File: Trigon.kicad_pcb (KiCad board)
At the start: 2 copper layers, 160 x 120 mm, 110 parts, among them J1 TYPE-C-31-M12_13, J2 TYPE-C-31-M12_13, SW1 SW_Push, SW2 Rotary_Encoder_Switch, U1 ATmega32U4-AU, U2 USBLC6-2SC6, U3 CY7C65632-28LTXCT, U4 USBLC6-2SC6, Y1 16MHz, Y2 12MHz

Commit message: next round of feedback from josh
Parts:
- removed D27, D28: 6V Breakdown, acheron_Components:D_SOD-123_Bidirectional
- moved R4 5.17 mm to (93.6, 20.6), turned to 0 degrees
- moved C2 2.06 mm to (146.3, 40.6)
- moved F1 1.83 mm to (96.6, 24.1)
- moved C21 1.83 mm to (97.4, 22.2)
- moved FB4 1.83 mm to (97.4, 26.0)
- moved C6 1.59 mm to (140.8, 44.2)
- moved C1 1.52 mm to (151.2, 43.2)
- moved R2 0.51 mm to (135.8, 56.4)
- moved R5 0.38 mm to (103.3, 23.4)
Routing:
- net +5V: track 237.0 -> 245.7 mm, vias 10 -> 9
- net GND: track 39.9 -> 48.3 mm, vias 28 -> 36
- net Net-(F1-Pad1): track 9.25 -> 2.84 mm
- net Net-(F2-Pad1): track 8.08 -> 2.50 mm
- net VBUS: track 19.0 -> 14.3 mm
- net Net-(J1-PadA5): track 3.65 -> 8.18 mm, vias 0 -> 2
- net ROW0: track 167.7 -> 170.9 mm, vias 6 -> 4
- net D3_D+: track 42.6 -> 44.5 mm
- net D3_D-: track 46.0 -> 47.9 mm
- net Net-(C2-Pad1): track 10.3 -> 8.68 mm
- net Net-(C1-Pad1): track 8.72 -> 7.19 mm
- net Net-(R10-Pad1): track 15.4 -> 16.2 mm
- net VREG_3V3: track 37.3 -> 38.2 mm
- net COL6: track 21.5 -> 22.3 mm
- net Net-(D13-Pad2): track 14.5 -> 15.3 mm
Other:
- board text added: "rev 0.1"
- board text removed: "rev 0"

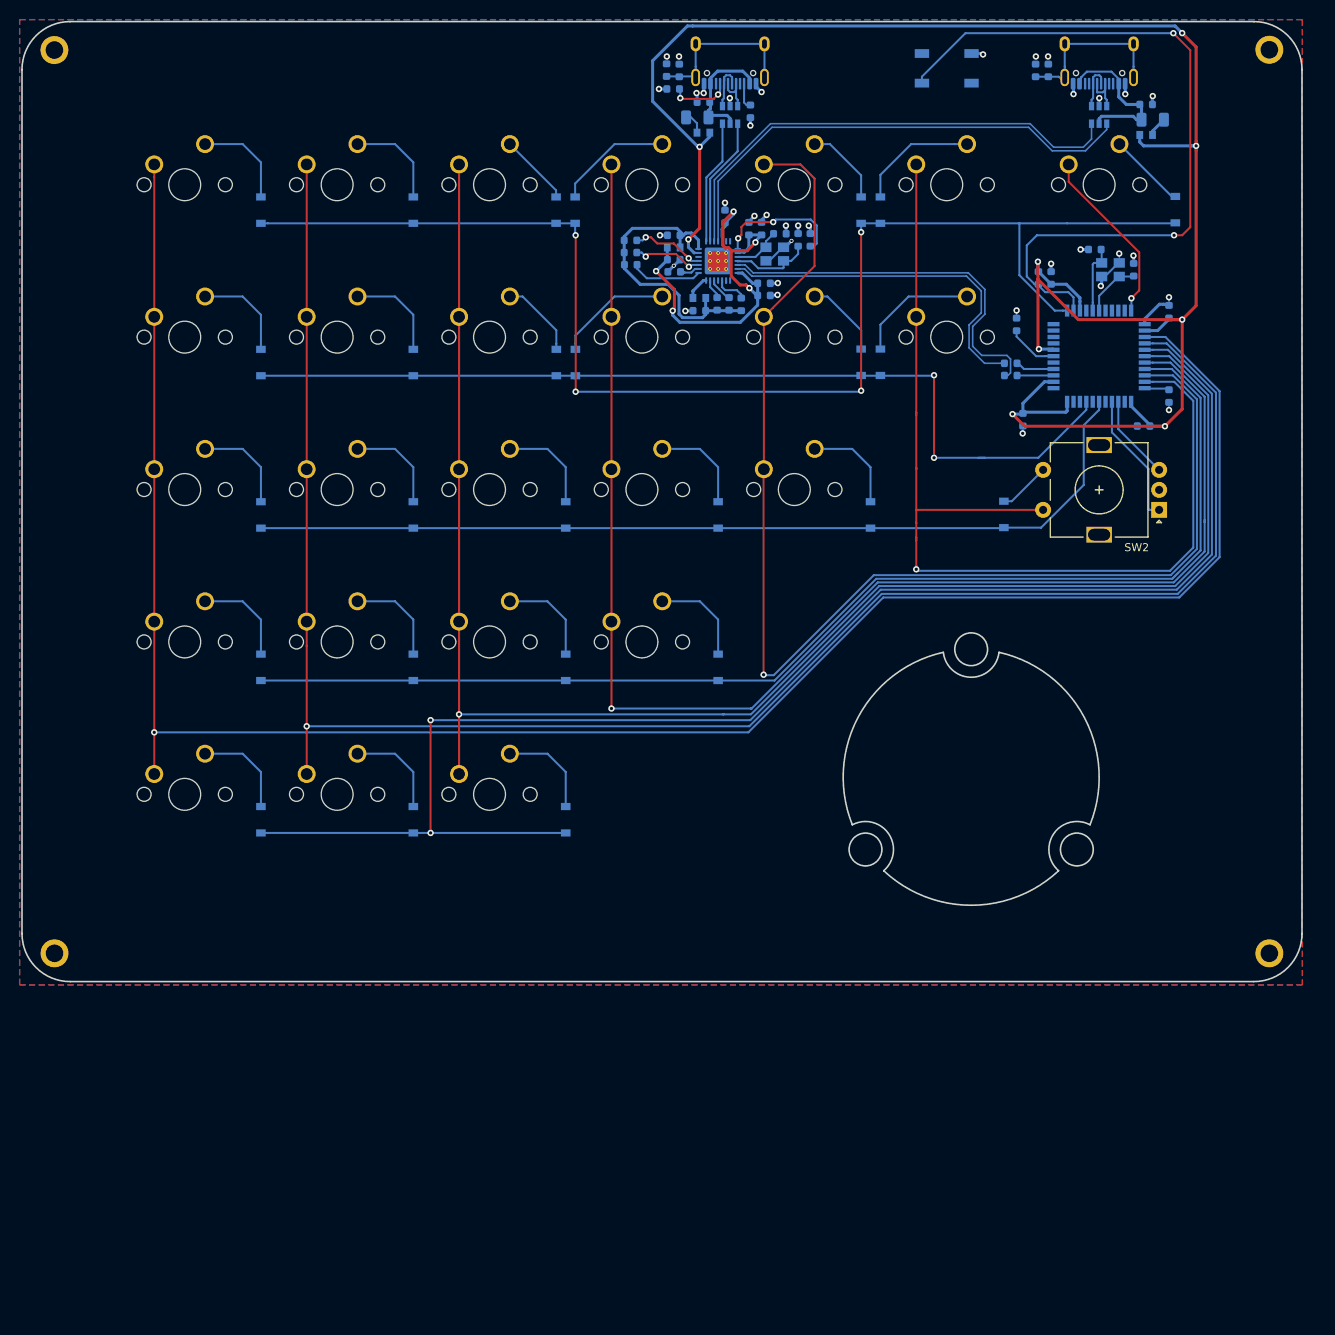
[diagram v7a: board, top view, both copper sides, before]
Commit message: - Introduced JST connector - Made all D+/D- 14mm thick (max thickness that was easy to deal with) - Added logo / decoration / version #
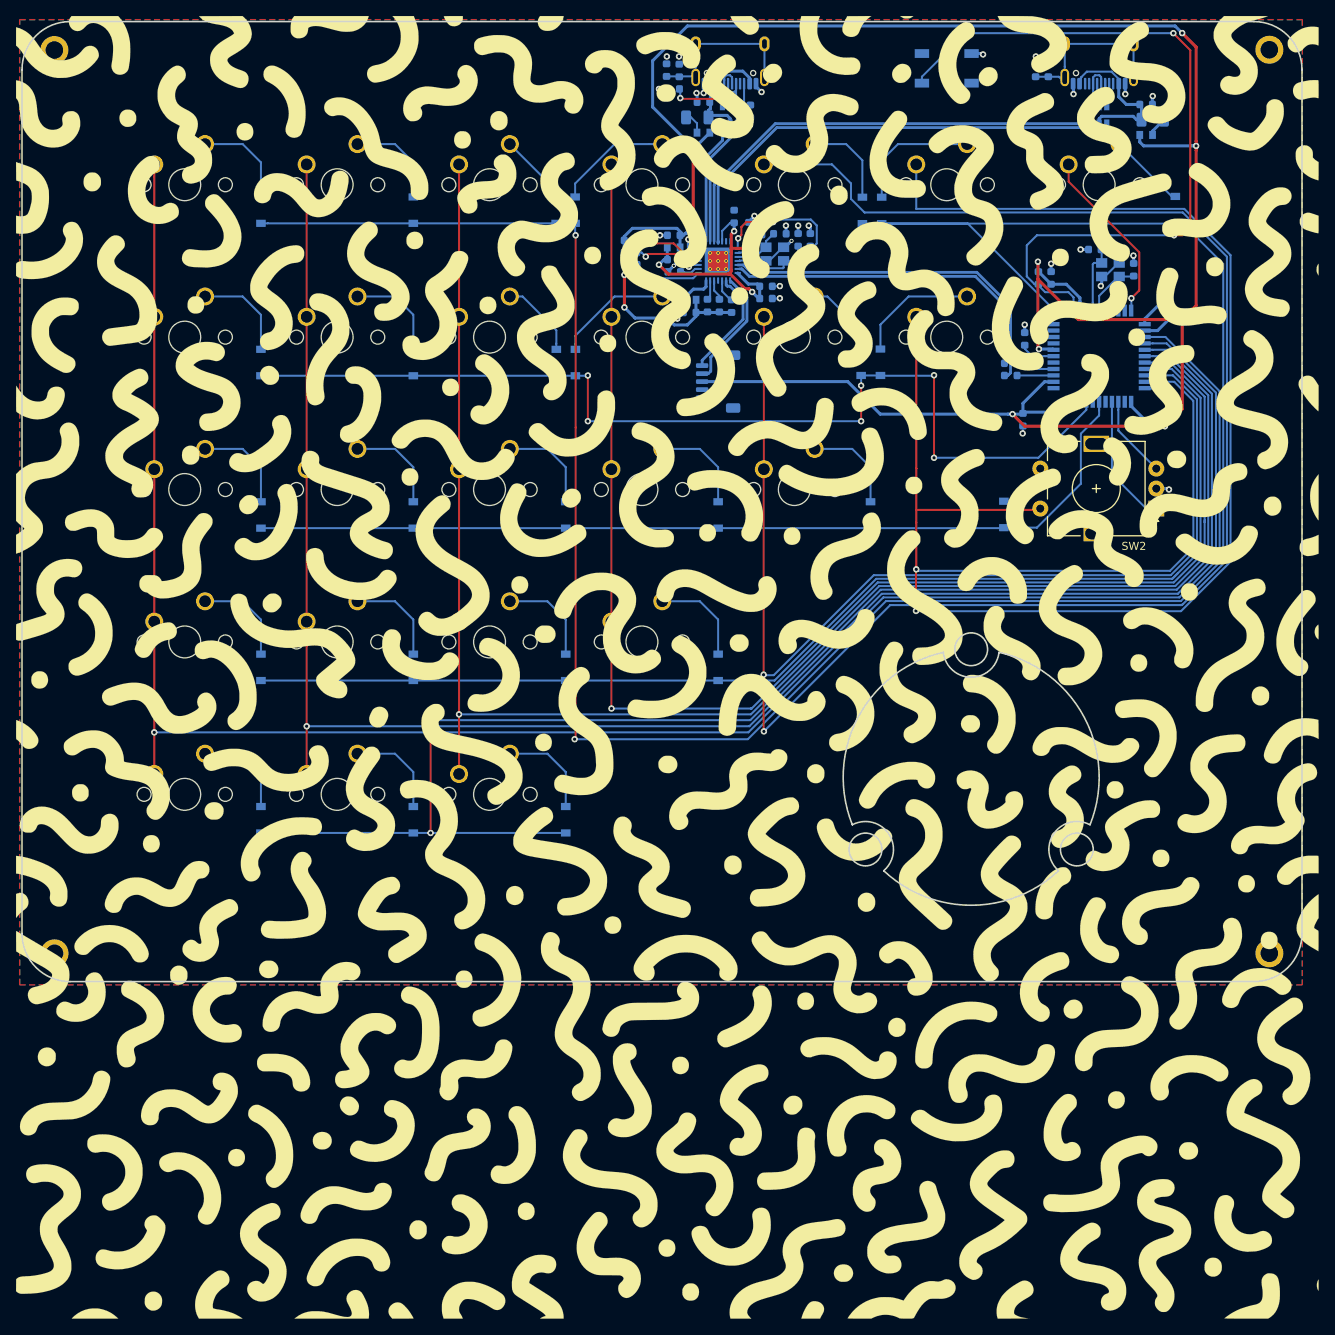
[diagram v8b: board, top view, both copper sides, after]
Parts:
- added H1: Logo, Trigon:wiggle, F.Cu at (92.9, 92.9)
- added J3: Conn_01x05, Connector_JST:JST_SH_SM05B-SRSS-TB_1x05-1MP_P1.00mm_Horizontal, B.Cu at (99.2, 57.1)
- SW2: footprint Keebio-Parts:RotaryEncoder_Alps_EC11E-Switch_Vertical_H20mm -> Rotary_Encoder:RotaryEncoder_Alps_EC11E-Switch_Vertical_H20mm
- moved SW2 7.52 mm to (154.0, 73.0)
- moved C3 2.08 mm to (137.5, 51.8)
- moved R13 1.23 mm to (97.9, 47.7)
- moved R14 1.23 mm to (99.4, 47.7)
- moved R9 1.23 mm to (100.9, 47.7)
- moved C8 1.23 mm to (95.7, 48.5)
- moved FB1 1.23 mm to (95.7, 46.9)
- moved C13 1.14 mm to (101.2, 36.5)
- moved C16 0.46 mm to (105.2, 46.8)
- moved C17 0.46 mm to (105.2, 45.2)
- moved D5 0.16 mm to (117.3, 35.8)
- moved D6 0.16 mm to (119.7, 35.8)
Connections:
- U3 pad 15: Net-(U3-Pad15) -> D2_D-
- U3 pad 16: Net-(U3-Pad16) -> D2_D+
- U3 pad 6: D2_D- -> Net-(U3-Pad6)
- U3 pad 7: D2_D+ -> Net-(U3-Pad7)
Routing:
- net COL4: track 159.8 -> 308.7 mm, vias 1 -> 2
- net ROW0: track 170.9 -> 306.1 mm, vias 4 -> 2
- net COL5: track 128.8 -> 242.9 mm, vias 1 -> 2
- net +5V: track 245.7 -> 286.3 mm
- net D2_D-: track 0.00 -> 15.3 mm
- net D2_D+: track 0.00 -> 13.8 mm
- net +3.3VA: track 55.2 -> 42.2 mm, vias 5 -> 4
- net ROW1: track 117.5 -> 128.9 mm, vias 2 -> 6
- net D1_D-: track 61.3 -> 57.4 mm
- net D3_D-: track 47.9 -> 45.5 mm
- net D3_D+: track 44.5 -> 42.4 mm
- net D1_D+: track 61.9 -> 60.0 mm
- net Net-(C3-Pad1): track 6.22 -> 4.43 mm
- net Net-(D5-Pad2): track 10.1 -> 11.4 mm
- net Net-(FB1-Pad1): track 3.06 -> 4.34 mm
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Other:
- net class USB Differential Pair added: clearance 0.127, trace_width 0.3556, via_dia 0.8, via_drill 0.4
- board text added: "nkultra"
- board text removed: "nk"
